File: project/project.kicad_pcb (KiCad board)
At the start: 2 copper layers, 85.5 x 85.5 mm, 79 parts, among them J101 IN, J102 1x7_5.08, J103 1x7_5.08, J104 1x7_5.08, J105 FFC, K1001 P6D-04P, K1101 P6D-04P, K1201 P6D-04P, K1301 P6D-04P, K1401 P6D-04P, K1501 P6D-04P, K1601 P6D-04P, K201 P6D-04P, K301 P6D-04P, K401 P6D-04P, K501 P6D-04P, K601 P6D-04P, K701 P6D-04P, K801 P6D-04P, K901 P6D-04P, Q1001 AO3400A, Q1101 AO3400A, Q1201 AO3400A, Q1301 AO3400A, Q1401 AO3400A, Q1501 AO3400A, Q1601 AO3400A, Q201 AO3400A, Q301 AO3400A, Q401 AO3400A, Q501 AO3400A, Q601 AO3400A, Q701 AO3400A, Q801 AO3400A, Q901 AO3400A, U101 GX101

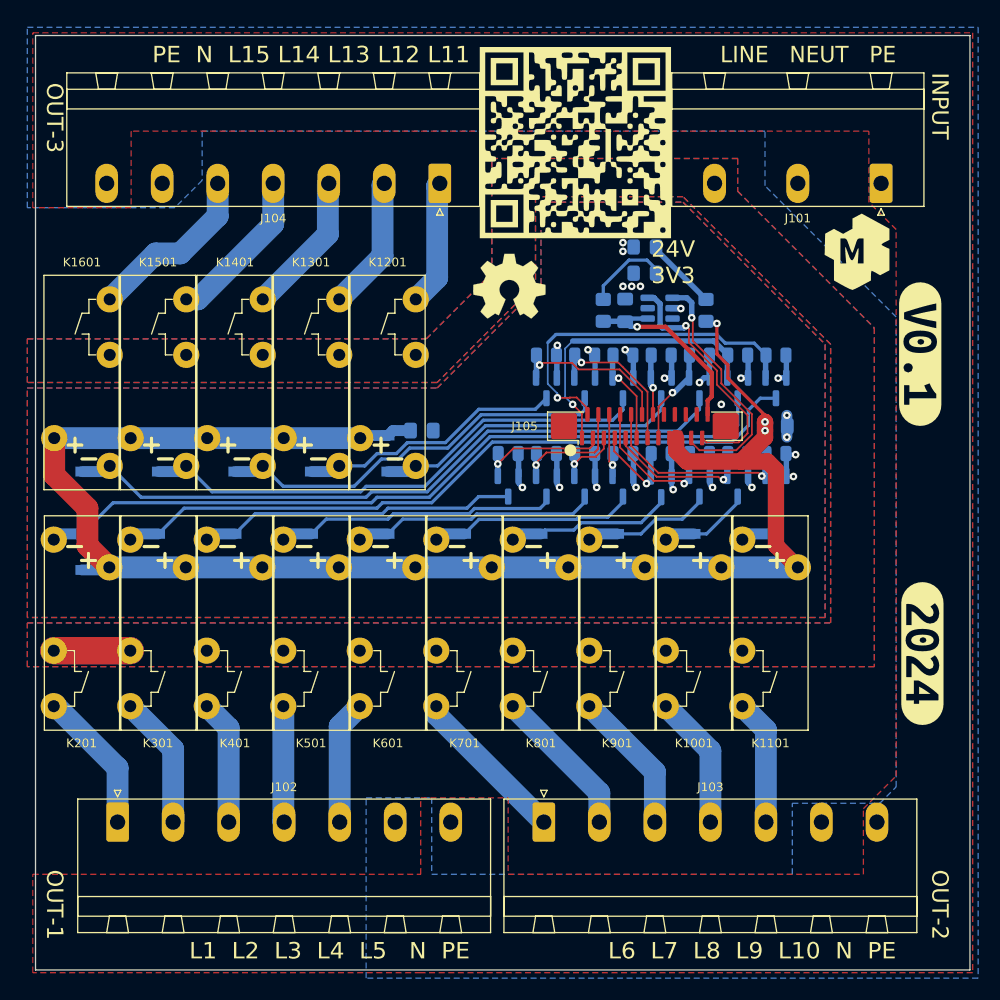
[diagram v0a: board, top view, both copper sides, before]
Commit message: removing fets as driving is upstairs now
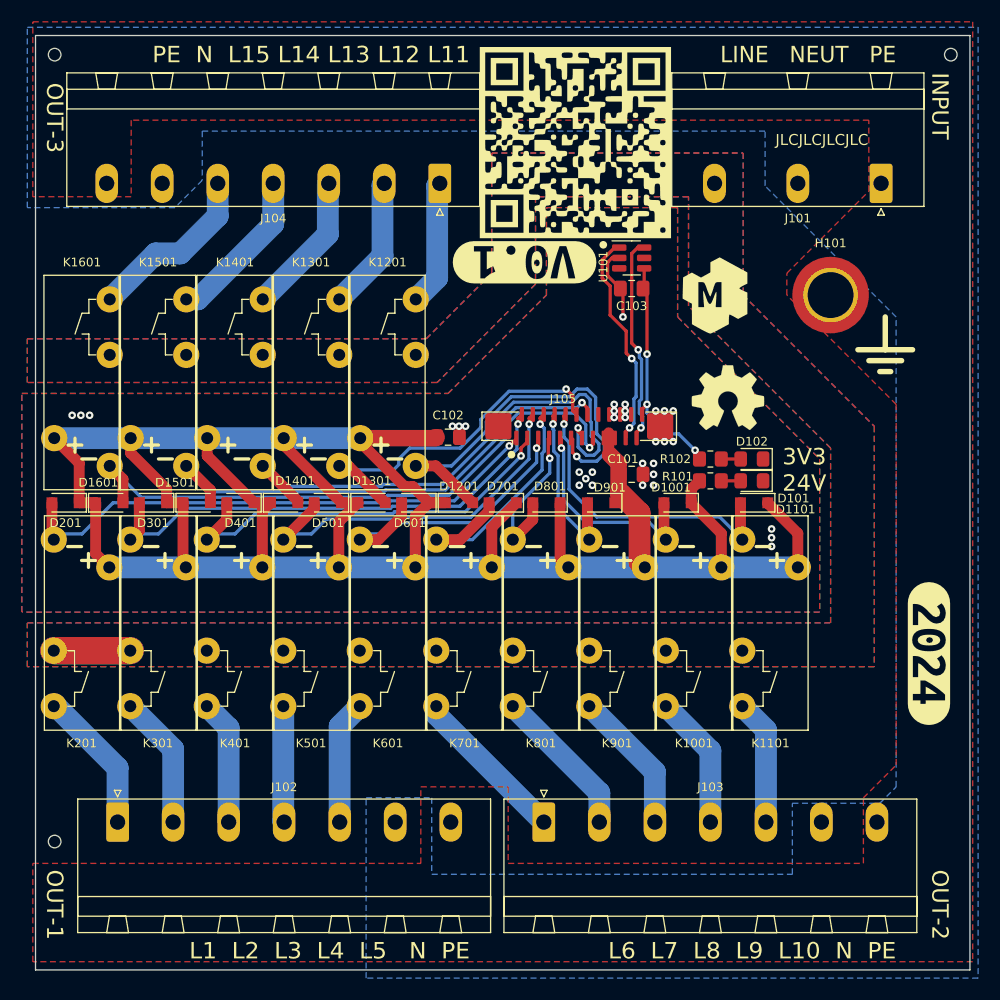
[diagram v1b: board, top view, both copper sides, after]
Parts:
- removed Q1001, Q1101, Q1201, Q1301, Q1401, Q1501, Q1601, Q201, Q301, Q401, Q501, Q601, Q701, Q801, Q901: AO3400A, Package_TO_SOT_SMD:SOT-23
- removed R1001, R1101, R1201, R1301, R1401, R1501, R1601, R201, R301, R401, R501, R601, R701, R801, R901: 10k, Resistor_SMD:R_0805_2012Metric
- added H101: M3, -local:post_m3x5mm, F.Cu at (198.3, 72.0)
- added REF**: toolhole, -local:toolhole, F.Cu at (127.3, 122.0)
- added REF**: toolhole, -local:toolhole, F.Cu at (127.3, 50.0)
- added REF**: toolhole, -local:toolhole, F.Cu at (209.3, 50.0)
- C101, C102, C103, R101, R102, U101: moved to F.Cu
- D1001, D1101, D1201, D1301, D1401, D1501, D1601, D201, D301, D401, D501, D601, D701, D801, D901: value B5819W -> B5819WS; footprint Diode_SMD:D_SOD-123 -> Diode_SMD:D_SOD-323_HandSoldering; moved to F.Cu
- D101: value 24V -> GREEN; moved to F.Cu
- D102: value 3V3 -> GREEN; moved to F.Cu
- J105: value FFC -> FFC Connector
- moved kibuzzard-6750110D 37.2 mm to (170.3, 69.0), turned to 180 degrees
- moved D101 23.5 mm to (191.1, 89.0), turned to 180 degrees
- moved G101 22.5 mm to (188.9, 81.4)
- moved D102 19.6 mm to (191.1, 87.0), turned to 180 degrees
- moved R102 16.8 mm to (187.3, 87.0), turned to 0 degrees
- moved R101 15.6 mm to (187.3, 89.0), turned to 0 degrees
- moved C101 13.9 mm to (180.1, 88.4)
- moved G102 13.6 mm to (187.3, 72.0)
- moved D1201 7.91 mm to (164.3, 91.0), turned to 0 degrees
- moved D1301 7.11 mm to (156.3, 91.0), turned to 0 degrees
- moved D1401 6.36 mm to (148.3, 91.0), turned to 0 degrees
- moved J105 6.00 mm to (175.3, 84.0)
- moved D1501 5.70 mm to (140.3, 91.0), turned to 0 degrees
- moved D701 5.70 mm to (168.3, 91.0), turned to 180 degrees
- moved U101 5.28 mm to (180.1, 68.6), turned to 0 degrees
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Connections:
- D1001 pad 2: Net-(D1001-Pad2) -> /_relay10/EN
- D1101 pad 2: Net-(D1101-Pad2) -> /_relay11/EN
- D1201 pad 2: Net-(D1201-Pad2) -> /_relay12/EN
- D1301 pad 2: Net-(D1301-Pad2) -> /_relay13/EN
- D1401 pad 2: Net-(D1401-Pad2) -> /_relay14/EN
- D1501 pad 2: Net-(D1501-Pad2) -> /_relay15/EN
- D1601 pad 2: Net-(D1601-Pad2) -> /_relay16/EN
- D201 pad 2: Net-(D201-Pad2) -> /_relay2/EN
- D301 pad 2: Net-(D301-Pad2) -> /_relay3/EN
- D401 pad 2: Net-(D401-Pad2) -> /_relay4/EN
- D501 pad 2: Net-(D501-Pad2) -> /_relay5/EN
- D601 pad 2: Net-(D601-Pad2) -> /_relay6/EN
- D701 pad 2: Net-(D701-Pad2) -> /_relay7/EN
- D801 pad 2: Net-(D801-Pad2) -> /_relay8/EN
- D901 pad 2: Net-(D901-Pad2) -> /_relay9/EN
- K1001 pad 1: Net-(D1001-Pad2) -> /_relay10/EN
- K1101 pad 1: Net-(D1101-Pad2) -> /_relay11/EN
- K1201 pad 1: Net-(D1201-Pad2) -> /_relay12/EN
- K1301 pad 1: Net-(D1301-Pad2) -> /_relay13/EN
- K1401 pad 1: Net-(D1401-Pad2) -> /_relay14/EN
- K1501 pad 1: Net-(D1501-Pad2) -> /_relay15/EN
- K1601 pad 1: Net-(D1601-Pad2) -> /_relay16/EN
- K201 pad 1: Net-(D201-Pad2) -> /_relay2/EN
- K301 pad 1: Net-(D301-Pad2) -> /_relay3/EN
- K401 pad 1: Net-(D401-Pad2) -> /_relay4/EN
- K501 pad 1: Net-(D501-Pad2) -> /_relay5/EN
- K601 pad 1: Net-(D601-Pad2) -> /_relay6/EN
- K701 pad 1: Net-(D701-Pad2) -> /_relay7/EN
- K801 pad 1: Net-(D801-Pad2) -> /_relay8/EN
- K901 pad 1: Net-(D901-Pad2) -> /_relay9/EN
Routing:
- net Net-(D201-Pad2): track 69.4 -> 0.00 mm
- net +24V: track 150.8 -> 219.3 mm, vias 3 -> 0
- net Net-(D301-Pad2): track 65.3 -> 0.00 mm
- net Net-(D1601-Pad2): track 62.3 -> 0.00 mm
- net Net-(D1501-Pad2): track 51.4 -> 0.00 mm
- net /_relay16/EN: track 8.84 -> 56.2 mm
- net GND: track 50.7 -> 6.81 mm, vias 25 -> 32
- net /_relay15/EN: track 6.53 -> 46.8 mm
- net Net-(D1401-Pad2): track 37.0 -> 0.00 mm
- net /_relay14/EN: track 15.3 -> 49.9 mm
- net Net-(D401-Pad2): track 29.2 -> 0.00 mm
- net /_relay12/EN: track 9.37 -> 37.2 mm
- net /_relay4/EN: track 12.2 -> 37.9 mm
- net Net-(D501-Pad2): track 25.5 -> 0.00 mm
- net Net-(D1201-Pad2): track 24.9 -> 0.00 mm
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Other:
- board text added: "3V3 24V"
- board text added: "JLCJLCJLCJLC"
- board text removed: "24V"
- board text removed: "24V 3V3"
- board text removed: "3V3"
